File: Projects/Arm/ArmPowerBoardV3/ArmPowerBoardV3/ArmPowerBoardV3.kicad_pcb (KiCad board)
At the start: 2 copper layers, 148.3 x 98.6 mm, 27 parts, among them J1 Screw_Terminal_01x04, J10 Atmega Holder, J11 Female Header R, J12 GPIO R, J13 JST serial, J2 Barrel_Jack, J3 Barrel_Jack, J4 Screw_Terminal_01x02, J5 Barrel_Jack, J6 Barrel_Jack, J7 Barrel_Jack, J8 Gpio L, J9 Femal header L, U1 ACS758, U2 VHB200W-Q24-S12, U3 25WDe-Swadj3, U4 Temp sense, Y1 Crystal

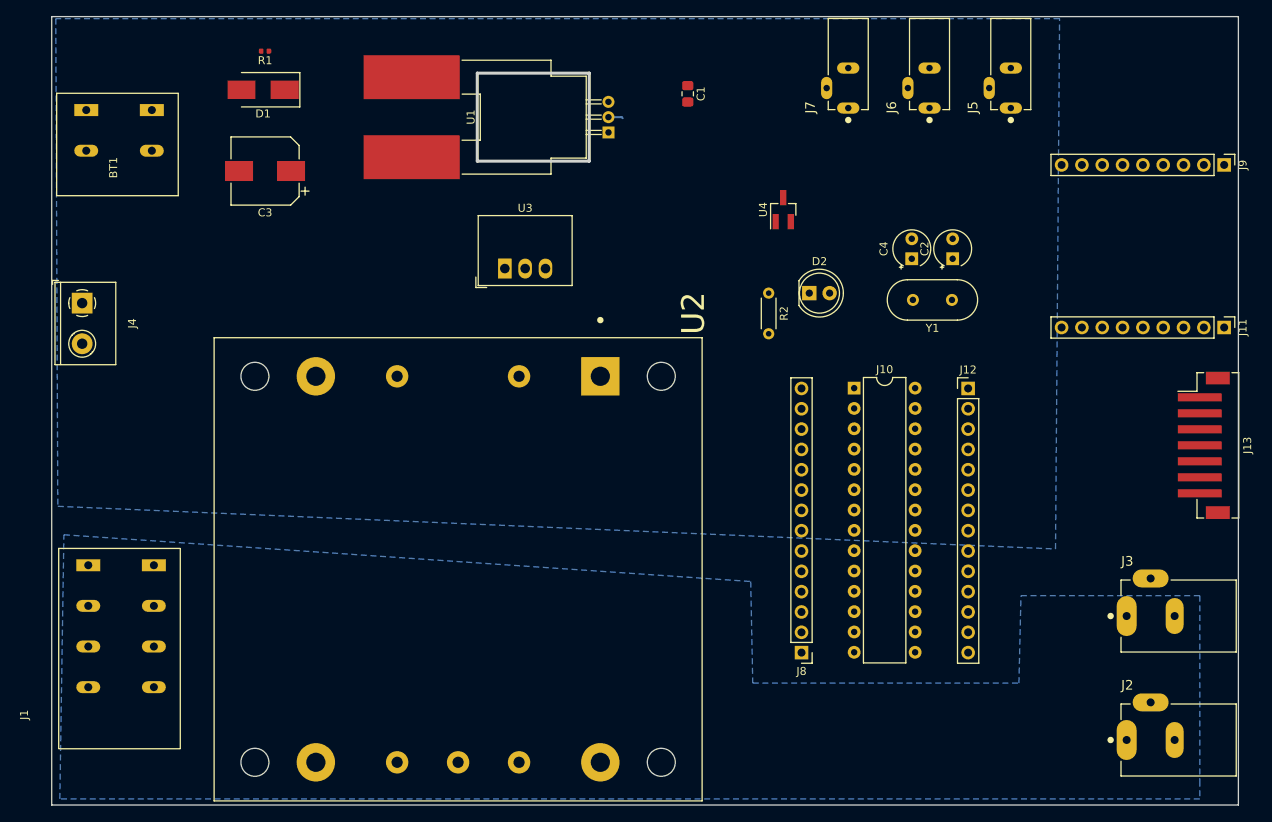
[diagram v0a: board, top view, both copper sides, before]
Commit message: work some more on the layout, had to move gpio for breakout board still need to hook those up and account for board mounting
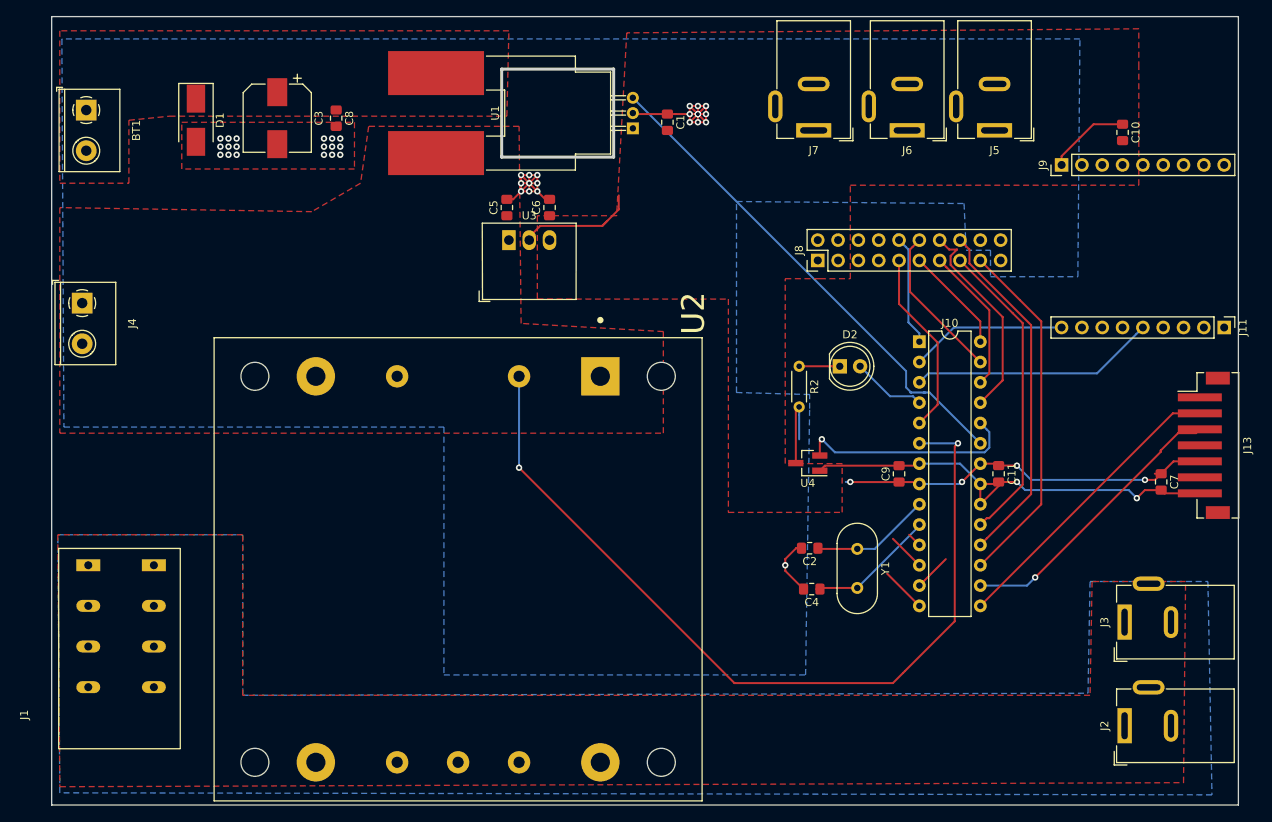
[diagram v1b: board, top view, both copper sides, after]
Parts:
- removed J12: GPIO R, Connector_PinHeader_2.54mm:PinHeader_1x14_P2.54mm_Vertical
- removed R1: 15ohm, Resistor_SMD:R_0402_1005Metric
- added C10: 100nF, Capacitor_SMD:C_0805_2012Metric_Pad1.15x1.40mm_HandSolder, F.Cu at (154.4, 46.7)
- added C11: 100nF, Capacitor_SMD:C_0805_2012Metric_Pad1.15x1.40mm_HandSolder, F.Cu at (138.9, 89.4)
- added C5: 10pF, Capacitor_SMD:C_0805_2012Metric_Pad1.15x1.40mm_HandSolder, F.Cu at (77.5, 56.1)
- added C6: 10pF, Capacitor_SMD:C_0805_2012Metric_Pad1.15x1.40mm_HandSolder, F.Cu at (82.8, 56.1)
- added C7: 100nF, Capacitor_SMD:C_0805_2012Metric_Pad1.15x1.40mm_HandSolder, F.Cu at (159.3, 90.4)
- added C8: 10 uF, Capacitor_SMD:C_0805_2012Metric_Pad1.15x1.40mm_HandSolder, F.Cu at (56.1, 45.0)
- added C9: 100nF, Capacitor_SMD:C_0805_2012Metric_Pad1.15x1.40mm_HandSolder, F.Cu at (126.5, 89.4)
- BT1: value 24V IN -> 24vin; footprint TerminalBlocks:TerminalBlock_Big2pin -> TerminalBlocks:TerminalBlock_1x02_P5.08mm_Horizontal
- C2, C4: footprint Capacitor_THT:CP_Radial_Tantal_D4.5mm_P2.50mm -> Capacitor_SMD:C_0805_2012Metric_Pad1.15x1.40mm_HandSolder
- J11: value Female Header R -> Breakout R
- J2, J3: footprint PJ-002BH:CUI_PJ-002BH -> Connector_BarrelJack:BarrelJack_Wuerth_6941xx301002
- J5, J6, J7: footprint PJ-007:CUI_PJ-007 -> Connector_BarrelJack:BarrelJack_Wuerth_6941xx301002
- J8: value Gpio L -> Gpio out; footprint Connector_PinHeader_2.54mm:PinHeader_1x14_P2.54mm_Vertical -> Connector_PinHeader_2.54mm:PinHeader_2x10_P2.54mm_Vertical
- J9: value Femal header L -> Breakout L
- U3: value 25WDe-Swadj3 -> V7805-1000; footprint Converter_DCDC:Converter_DCDC_RECOM_R-78HBxx-0.5_THT -> TerminalBlocks:V7805-1000
- moved J8 49.1 mm to (116.3, 62.7), turned to 90 degrees
- moved C4 43.1 mm to (115.6, 103.8), turned to 180 degrees
- moved C2 40.4 mm to (115.3, 98.7), turned to 180 degrees
- moved Y1 33.3 mm to (121.3, 98.8), turned to 270 degrees
- moved U4 31.8 mm to (115.1, 88.1), turned to 180 degrees
- moved J9 20.3 mm to (146.8, 50.8), turned to 90 degrees
- moved J10 10.0 mm to (129.0, 72.9)
- moved D2 9.91 mm to (119.1, 76.0)
- moved R2 9.91 mm to (114.0, 76.0)
- moved D1 9.21 mm to (38.6, 45.2), turned to 270 degrees
- moved C3 6.78 mm to (48.8, 45.0), turned to 270 degrees
- moved J7 5.14 mm to (115.8, 46.5), turned to 180 degrees
- moved C1 4.37 mm to (97.5, 45.5)
- moved J6 3.95 mm to (127.5, 46.5), turned to 180 degrees
- moved U3 3.59 mm to (77.7, 60.2)
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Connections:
- BT1 pad 1: Net-(BT1-Pad1) -> GND
- BT1 pad 2: GND -> Net-(BT1-Pad2)
- C1 pad 2: 5vPS -> 5v+
- C3 pad 1: Net-(C3-Pad1) -> Net-(BT1-Pad2)
- D1 pad 1: Net-(C3-Pad1) -> Net-(BT1-Pad2)
- D2 pad 2: 5vPS -> Net-(D2-Pad2)
- J10 pad 20: 5vPS -> 5v+
- J10 pad 21: 5vPS -> 5v+
- J10 pad 4: Net-(J10-Pad4) -> Net-(D2-Pad2)
- J10 pad 6: Net-(J10-Pad6) -> ONoff
- J10 pad 7: 5vPS -> 5v+
- J13 pad 5: (no net) -> GND
- J13 pad 7: (no net) -> 5v+
- J5 pad 1: 5vPS -> 5v+
- J6 pad 1: 5vPS -> 5v+
- J7 pad 1: 5vPS -> 5v+
- J8 pad 1: Net-(J10-Pad14) -> 5v+
- J8 pad 10: Net-(J10-Pad5) -> Net-(J10-Pad1)
- J8 pad 11: Net-(J10-Pad4) -> Net-(J10-Pad28)
- J8 pad 12: (no net) -> Net-(J10-Pad27)
- J8 pad 13: (no net) -> Net-(J10-Pad26)
- J8 pad 14: Net-(J10-Pad1) -> Net-(J10-Pad25)
- J8 pad 2: Net-(J10-Pad13) -> 5v+
- J8 pad 3: Net-(J10-Pad12) -> 5v+
- J8 pad 4: Net-(J10-Pad11) -> 5v+
- J8 pad 5: (no net) -> Net-(J10-Pad14)
- J8 pad 6: (no net) -> Net-(J10-Pad13)
- J8 pad 7: (no net) -> Net-(J10-Pad12)
- J8 pad 8: (no net) -> Net-(J10-Pad11)
- J8 pad 9: Net-(J10-Pad6) -> Net-(J10-Pad5)
- J9 pad 1: (no net) -> GND
- J9 pad 4: (no net) -> 5v+
- U1 pad 1: 5vPS -> 5v+
- U1 pad 4: Net-(C3-Pad1) -> Net-(BT1-Pad2)
- U2 pad 2: (no net) -> ONoff
- U3 pad 3: 5vPS -> 5v+
- U4 pad 1: 5vPS -> 5v+
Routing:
- net GND: track 1.83 -> 139.8 mm, vias 0 -> 42
- net ONoff: track 0.00 -> 107.5 mm, vias 0 -> 2
- net ISense: track 0.00 -> 62.9 mm
- net 5v+: track 0.00 -> 56.7 mm, vias 0 -> 2
- net Net-(J10-Pad18): track 0.00 -> 44.4 mm
- net Net-(J10-Pad17): track 0.00 -> 44.4 mm
- net Net-(J10-Pad19): track 0.00 -> 38.6 mm
- net RX1: track 0.00 -> 37.4 mm
- net TX1: track 0.00 -> 35.6 mm, vias 0 -> 1
- net Tx: track 0.00 -> 30.8 mm
- net TempSense: track 0.00 -> 27.5 mm, vias 0 -> 1
- net Net-(J10-Pad25): track 0.00 -> 26.0 mm
- net Net-(J10-Pad5): track 0.00 -> 23.3 mm
- net Rx: track 0.00 -> 19.6 mm
- net Net-(J10-Pad27): track 0.00 -> 19.4 mm
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- added copper zone on F.Cu, net 12v+
- added copper zone on F.Cu, net 24v
- added copper zone on F.Cu, net 5v+
- added copper zone on F.Cu, net GND
- added copper zone on F.Cu, net Net-(BT1-Pad2)

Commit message: Added three screw holes, position was just wherever felt free
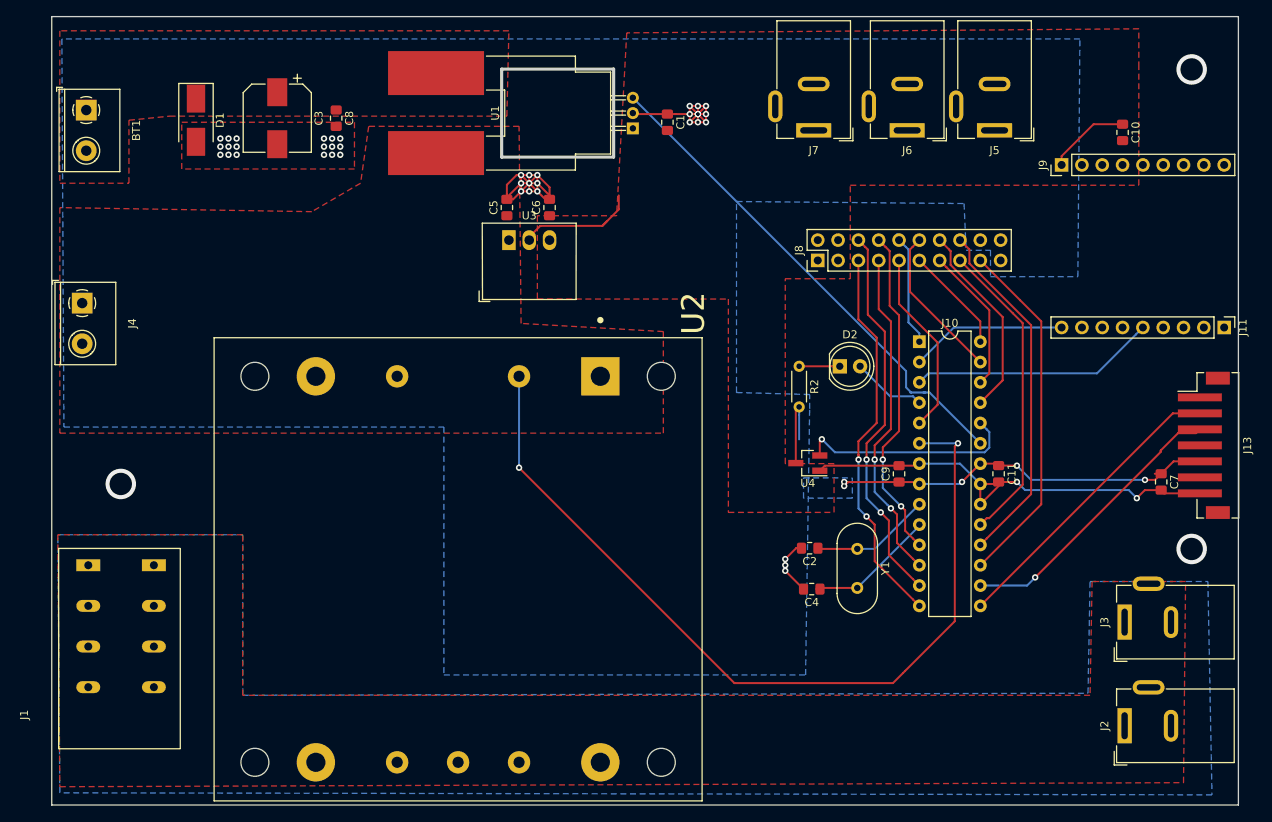
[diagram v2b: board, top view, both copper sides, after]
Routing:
- net Net-(J10-Pad13): track 4.67 -> 48.2 mm, vias 0 -> 2
- net Net-(J10-Pad14): track 5.70 -> 48.2 mm, vias 0 -> 2
- net Net-(J10-Pad11): track 1.80 -> 41.9 mm, vias 0 -> 2
- net Net-(J10-Pad12): track 4.67 -> 41.9 mm, vias 0 -> 2
- net GND: track 139.8 -> 154.3 mm, vias 42 -> 45
- net Net-(J10-Pad25): track 26.0 -> 24.7 mm
- net (no net): vias 0 -> 3

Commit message: Touched up the PCB Layout, Generated Gerber/Drill Files
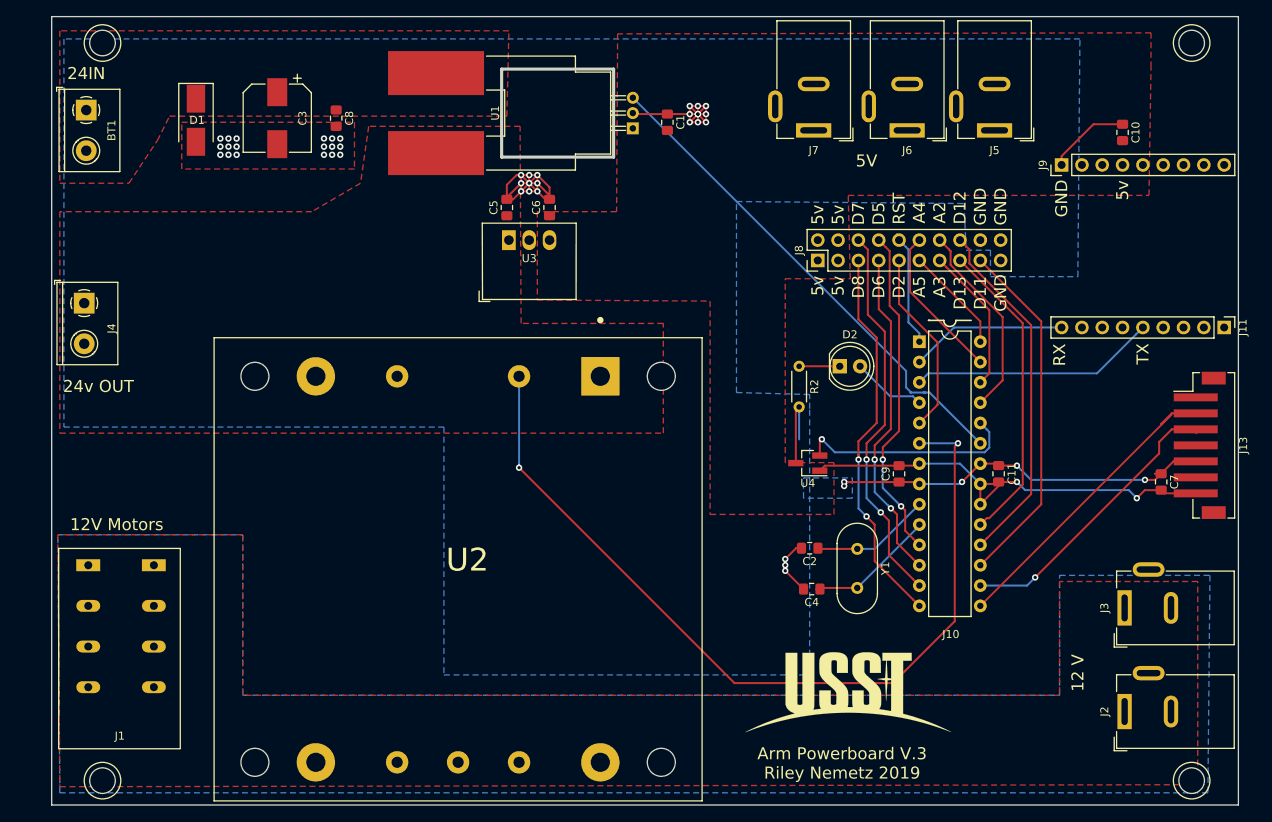
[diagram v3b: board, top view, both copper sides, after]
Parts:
- added G***: LOGO, USSTlogo:USSTLOGO, F.Cu at (120.1, 116.7)
- added REF**: MountingHole, ScrewMount:MountingHole, F.Cu at (26.9, 35.6)
- added REF**: MountingHole, ScrewMount:MountingHole, F.Cu at (26.9, 127.8)
- added REF**: MountingHole, ScrewMount:MountingHole, F.Cu at (163.1, 127.8)
- added REF**: MountingHole, ScrewMount:MountingHole, F.Cu at (163.1, 35.6)
- moved J3 1.78 mm to (154.7, 106.2)
- moved J2 1.78 mm to (154.7, 119.1)
- moved J13 0.51 mm to (164.1, 85.9)
- moved J4 0.25 mm to (24.6, 68.1)
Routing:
- net GND: track 154.3 -> 139.1 mm
- net RX1: track 37.4 -> 38.8 mm
- net TX1: track 35.6 -> 36.5 mm
- net (no net): vias 3 -> 0
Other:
- board text added: "12 V"
- board text added: "12V"
- board text added: "12V Motors"
- board text added: "24IN"
- board text added: "24V"
- board text added: "24v OUT"
- board text added: "5V"
- board text added: "5v"
- board text added: "A2"
- board text added: "A3"
- board text added: "A4"
- board text added: "A5"
- board text added: "Arm Powerboard V.3 Riley Nemetz 2019"
- board text added: "D11"
- board text added: "D12"
- board text added: "D13"
- board text added: "D2"
- board text added: "D5"
- board text added: "D6"
- board text added: "D7"
- board text added: "D8"
- board text added: "GND"
- board text added: "RST"
- board text added: "RX"
- board text added: "TX"
